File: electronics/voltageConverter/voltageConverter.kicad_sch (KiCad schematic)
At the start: 9 parts

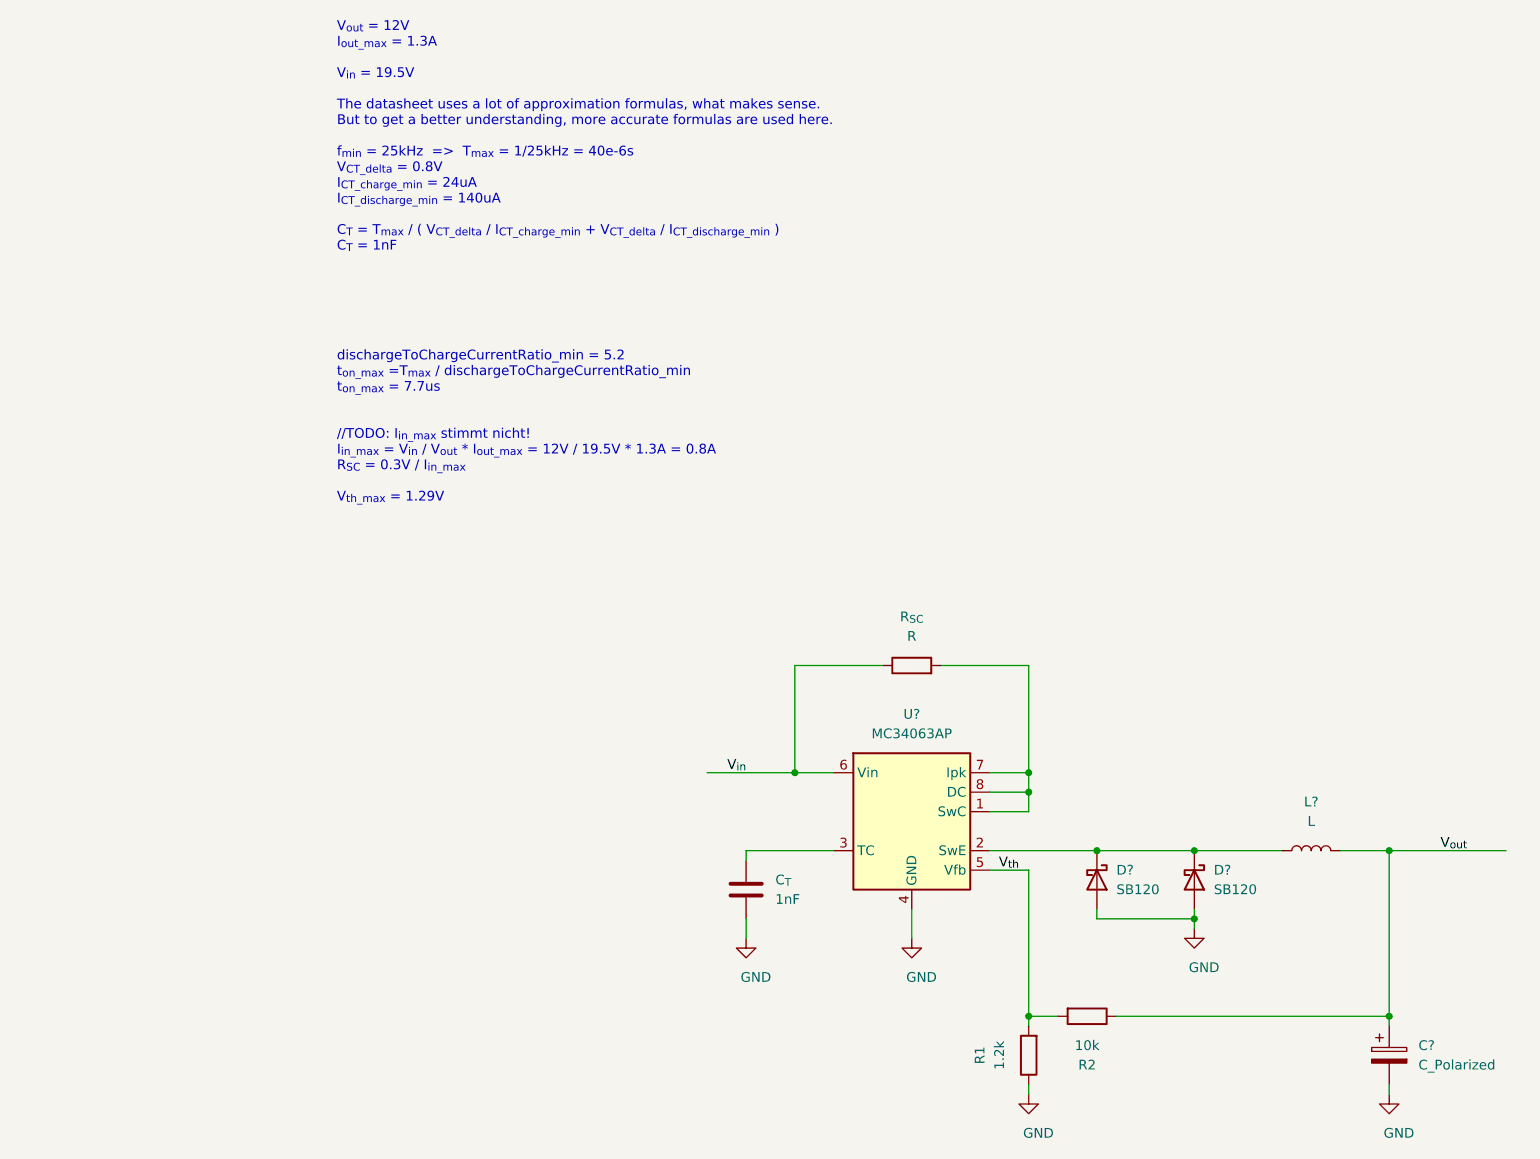
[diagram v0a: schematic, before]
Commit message: more parts calculated
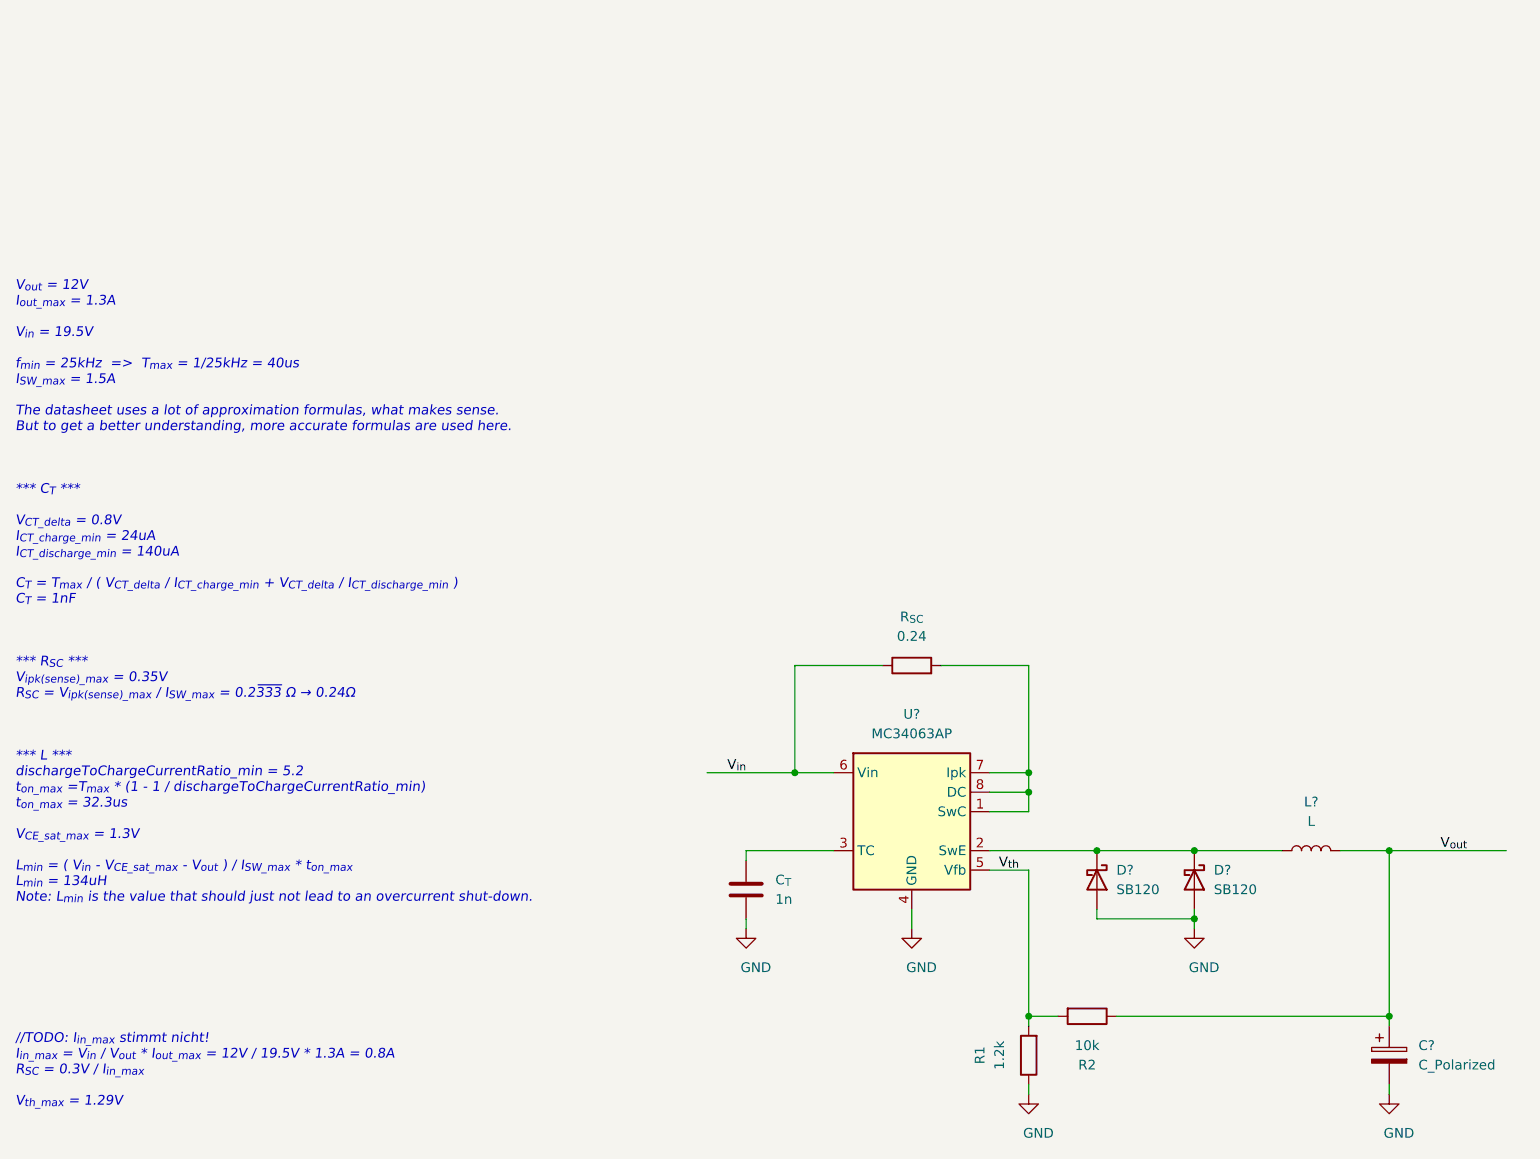
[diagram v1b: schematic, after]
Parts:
- C_{T}: value 1nF -> 1n
- R_{SC}: value R -> 0.24
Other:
- note added: "V_{out} = 12V I_{out_max} = 1.3A V_{in} = 19.5V f_{min} = 25kHz => T_{max} = 1/25kHz = 40us I_{SW_max} = 1.5A The datasheet uses a lot of approximation formulas, what makes sense. But to get a better understanding, more accurate formulas are used here. *** C_{T} *** V_{CT_delta} = 0.8V I_{CT_charge_min} = 24uA I_{CT_discharge_min} = 140uA C_{T} = T_{max} / ( V_{CT_delta} / I_{CT_charge_min} + V_{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"
- note removed: "V_{out} = 12V I_{out_max} = 1.3A V_{in} = 19.5V The datasheet uses a lot of approximation formulas, what makes sense. But to get a better understanding, more accurate formulas are used here. f_{min} = 25kHz => T_{max} = 1/25kHz = 40e-6s V_{CT_delta} = 0.8V I_{CT_charge_min} = 24uA I_{CT_discharge_min} = 140uA C_{T} = T_{max} / ( V_{CT_delta} / I_{CT_charge_min} + V_{CT_delta} / I_{CT_discharge_mi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"
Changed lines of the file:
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@@
     (stroke (width 0) (type solid) (color 0 0 0 0))
   )
-  (wire (pts (xy 138.43 101.6) (xy 138.43 104.14))
+  (wire (pts (xy 138.43 101.6) (xy 138.43 102.87))
     (stroke (width 0) (type solid) (color 0 0 0 0))
   )
@@
     (stroke (width 0) (type solid) (color 0 0 0 0))
   )
-  (wire (pts (xy 160.02 100.33) (xy 160.02 104.14))
+  (wire (pts (xy 160.02 100.33) (xy 160.02 102.87))
     (stroke (width 0) (type solid) (color 0 0 0 0))
   )
@@
     (stroke (width 0) (type solid) (color 0 0 0 0))
   )
-  (text "V_{out} = 12V\nI_{out_max} = 1.3A\n\nV_{in} = 19.5V\n\nThe datasheet uses a lot of approximation formulas, what makes sense.\nBut to get a better understanding, more accurate formulas are used here.\n\nf_{min} = 25kHz  =>  T_{max} = 1/25kHz = 40e-6s\nV_{CT_delta} = 0.8V\nI_{CT_charge_min} = 24uA\nI_{CT_discharge_min} = 140uA\n\nC_{T} = T_{max} / ( V_{CT_delta} / I_{CT_charge_min} + V_{CT_delta} / I_{CT_discharge_min} )\nC_{T} = 1nF\n\n\n\n\n\n\ndischargeToChargeCurrentRatio_min = 5.2\nt_{on_max} =T_{max} / dischargeToChargeCurrentRatio_min\nt_{on_max} = 7.7us \n\n\n//TODO: I_{in_max} stimmt nicht!\nI_{in_max} = V_{in} / V_{out} * I_{out_max} = 12V / 19.5V * 1.3A = 0.8A\nR_{SC} = 0.3V / I_{in_max}\n\nV_{th_max} = 1.29V\n\n"
-    (at 85.09 49.53 0)
-    (effects (font (size 1.27 1.27)) (justify left bottom))
+  (text "V_{out} = 12V\nI_{out_max} = 1.3A\n\nV_{in} = 19.5V\n\nf_{min} = 25kHz  =>  T_{max} = 1/25kHz = 40us\nI_{SW_max} = 1.5A\n\nThe datasheet uses a lot of approximation formulas, what makes sense.\nBut to get a better understanding, more accurate formulas are used here.\n\n\n\n*** C_{T} ***\n\nV_{CT_delta} = 0.8V\nI_{CT_charge_min} = 24uA\nI_{CT_discharge_min} = 140uA\n\nC_{T} = T_{max} / ( V_{CT_delta} / I_{CT_charge_min} + V_{CT_delta} / I_{CT_discharge_min} )\nC_{T} = 1nF\n\n\n\n*** R_{SC} ***\nV_{ipk(sense)_max} = 0.35V\nR_{SC} = V_{ipk(sense)_max} / I_{SW_max} = 0.2~333 Ω → 0.24Ω\n\n\n\n*** L ***\ndischargeToChargeCurrentRatio_min = 5.2\nt_{on_max} =T_{max} * (1 - 1 / dischargeToChargeCurrentRatio_min)\nt_{on_max} = 32.3us \n\nV_{CE_sat_max} = 1.3V\n\nL_{min} = ( V_{in} - V_{CE_sat_max} - V_{out} ) / I_{SW_max} * t_{on_max}\nL_{min} = 134uH\nNote: L_{min} is the value that should just not lead to an overcurrent shut-down.\n\n\n\n\n\n\n\n\n//TODO: I_{in_max} stimmt nicht!\nI_{in_max} = V_{in} / V_{out} * I_{out_max} = 12V / 19.5V * 1.3A = 0.8A\nR_{SC} = 0.3V / I_{in_max}\n\nV_{th_max} = 1.29V\n\n"
+    (at 43.18 128.27 0)
+    (effects (font (size 1.27 1.27) italic) (justify left bottom))
   )
   (label "V_{in}" (at 138.43 82.55 180)
@@
     )
   )
-  (symbol (lib_id "power:GND") (at 138.43 104.14 0) (unit 1)
-    (in_bom yes) (on_board yes)
-    (property "Reference" "#PWR?" (id 0) (at 138.43 110.49 0)
-      (effects (font (size 1.27 1.27)) hide)
-    )
-    (property "Value" "GND" (id 1) (at 139.7 109.22 0))
-    (property "Footprint" "" (id 2) (at 138.43 104.14 0)
-      (effects (font (size 1.27 1.27)) hide)
-    )
-    (property "Datasheet" "" (id 3) (at 138.43 104.14 0)
-      (effects (font (size 1.27 1.27)) hide)
-    )
-  )
-  (symbol (lib_id "power:GND") (at 160.02 104.14 0) (unit 1)
-    (in_bom yes) (on_board yes)
-    (property "Reference" "#PWR?" (id 0) (at 160.02 110.49 0)
-      (effects (font (size 1.27 1.27)) hide)
-    )
-    (property "Value" "GND" (id 1) (at 161.29 109.22 0))
-    (property "Footprint" "" (id 2) (at 160.02 104.14 0)
-      (effects (font (size 1.27 1.27)) hide)
-    )
-    (property "Datasheet" "" (id 3) (at 160.02 104.14 0)
+  (symbol (lib_id "power:GND") (at 138.43 102.87 0) (unit 1)
+    (in_bom yes) (on_board yes)
+    (property "Reference" "#PWR?" (id 0) (at 138.43 109.22 0)
+      (effects (font (size 1.27 1.27)) hide)
+    )
+    (property "Value" "GND" (id 1) (at 139.7 107.95 0))
+    (property "Footprint" "" (id 2) (at 138.43 102.87 0)
+      (effects (font (size 1.27 1.27)) hide)
+    )
+    (property "Datasheet" "" (id 3) (at 138.43 102.87 0)
+      (effects (font (size 1.27 1.27)) hide)
+    )
+  )
+  (symbol (lib_id "power:GND") (at 160.02 102.87 0) (unit 1)
+    (in_bom yes) (on_board yes)
+    (property "Reference" "#PWR?" (id 0) (at 160.02 109.22 0)
+      (effects (font (size 1.27 1.27)) hide)
+    )
+    (property "Value" "GND" (id 1) (at 161.29 107.95 0))
+    (property "Footprint" "" (id 2) (at 160.02 102.87 0)
+      (effects (font (size 1.27 1.27)) hide)
+    )
+    (property "Datasheet" "" (id 3) (at 160.02 102.87 0)
       (effects (font (size 1.27 1.27)) hide)
     )
@@
     (in_bom yes) (on_board yes)
     (property "Reference" "R_{SC}" (id 0) (at 160.02 62.23 90))
-    (property "Value" "R" (id 1) (at 160.02 64.77 90))
+    (property "Value" "0.24" (id 1) (at 160.02 64.77 90))
     (property "Footprint" "" (id 2) (at 160.02 70.358 90)
       (effects (font (size 1.27 1.27)) hide)
@@
       (effects (font (size 1.27 1.27)) (justify left))
     )
-    (property "Value" "1nF" (id 1) (at 142.24 99.06 0)
+    (property "Value" "1n" (id 1) (at 142.24 99.06 0)
       (effects (font (size 1.27 1.27)) (justify left))
     )
@@
     )
     (path "/8bc0df8a-4b0a-434f-a815-2bbffbc48f9a"
-      (reference "C_{T}") (unit 1) (value "1nF") (footprint "")
+      (reference "C_{T}") (unit 1) (value "1n") (footprint "")
     )
     (path "/1d417eb0-09ee-41de-81bb-b29e446a28bc"
@@
     )
     (path "/70557cb0-995e-4a06-8132-32edc28303b2"
-      (reference "R_{SC}") (unit 1) (value "R") (footprint "")
+      (reference "R_{SC}") (unit 1) (value "0.24") (footprint "")
     )
     (path "/ac246f61-9aaf-4e1f-995d-13986233ee56"
